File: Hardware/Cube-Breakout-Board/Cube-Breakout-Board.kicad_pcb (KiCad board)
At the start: 2 copper layers, 72.1 x 102.6 mm, 9 parts, among them J1 Pixhawk_Cube_DF17_80_Pin_Grou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, J2 Pixhawk_Cube_DF17_80_Pin_Grou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, J3 Conn_01x30, J4 Conn_01x22, J5 Conn_01x30

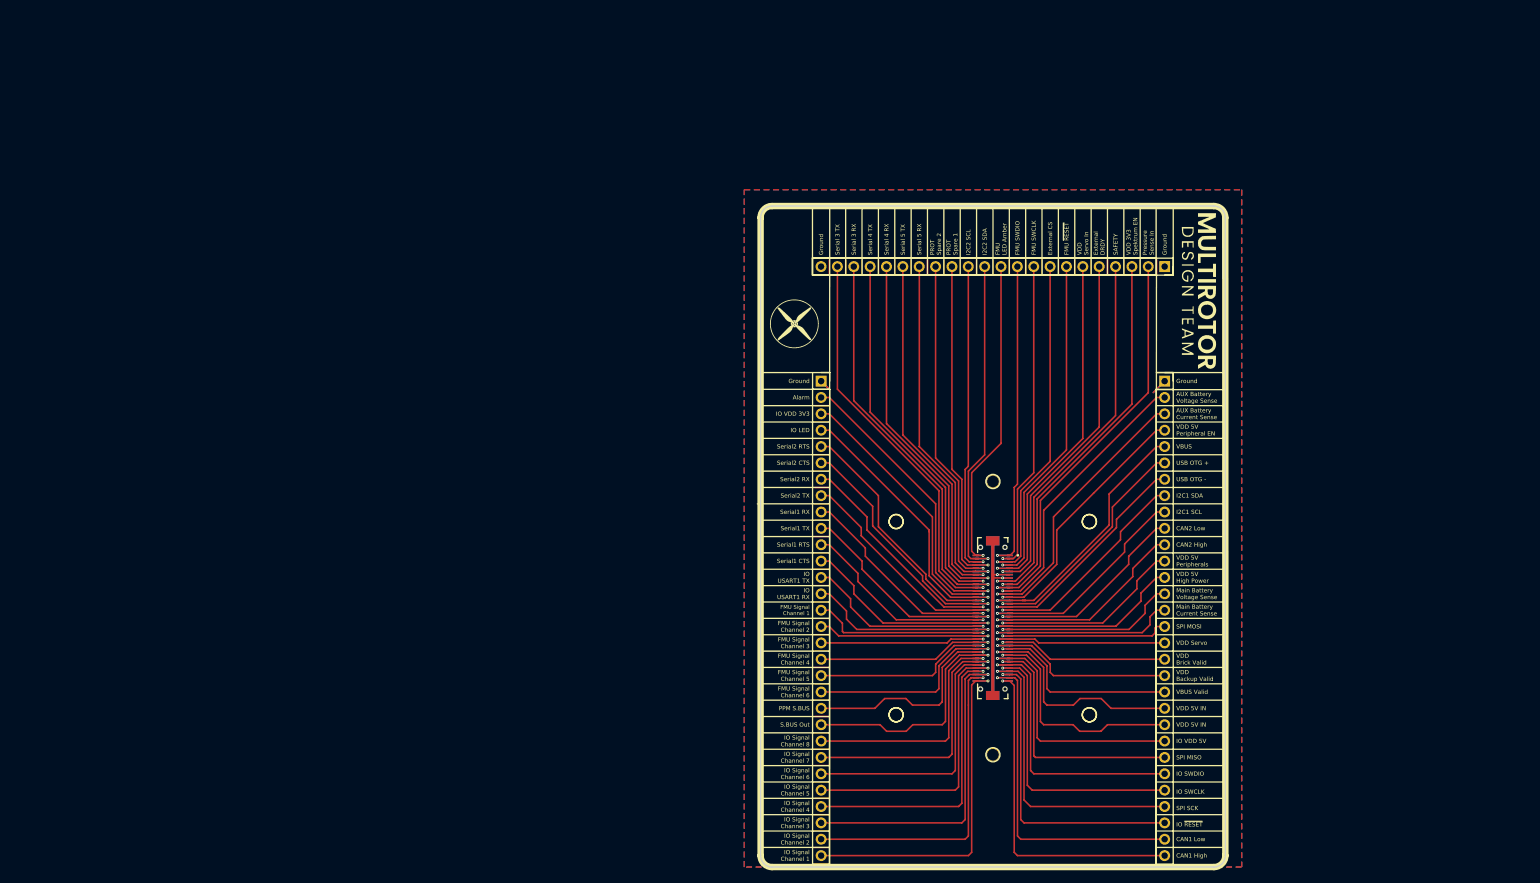
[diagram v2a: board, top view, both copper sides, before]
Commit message: Added dimensions to PCB
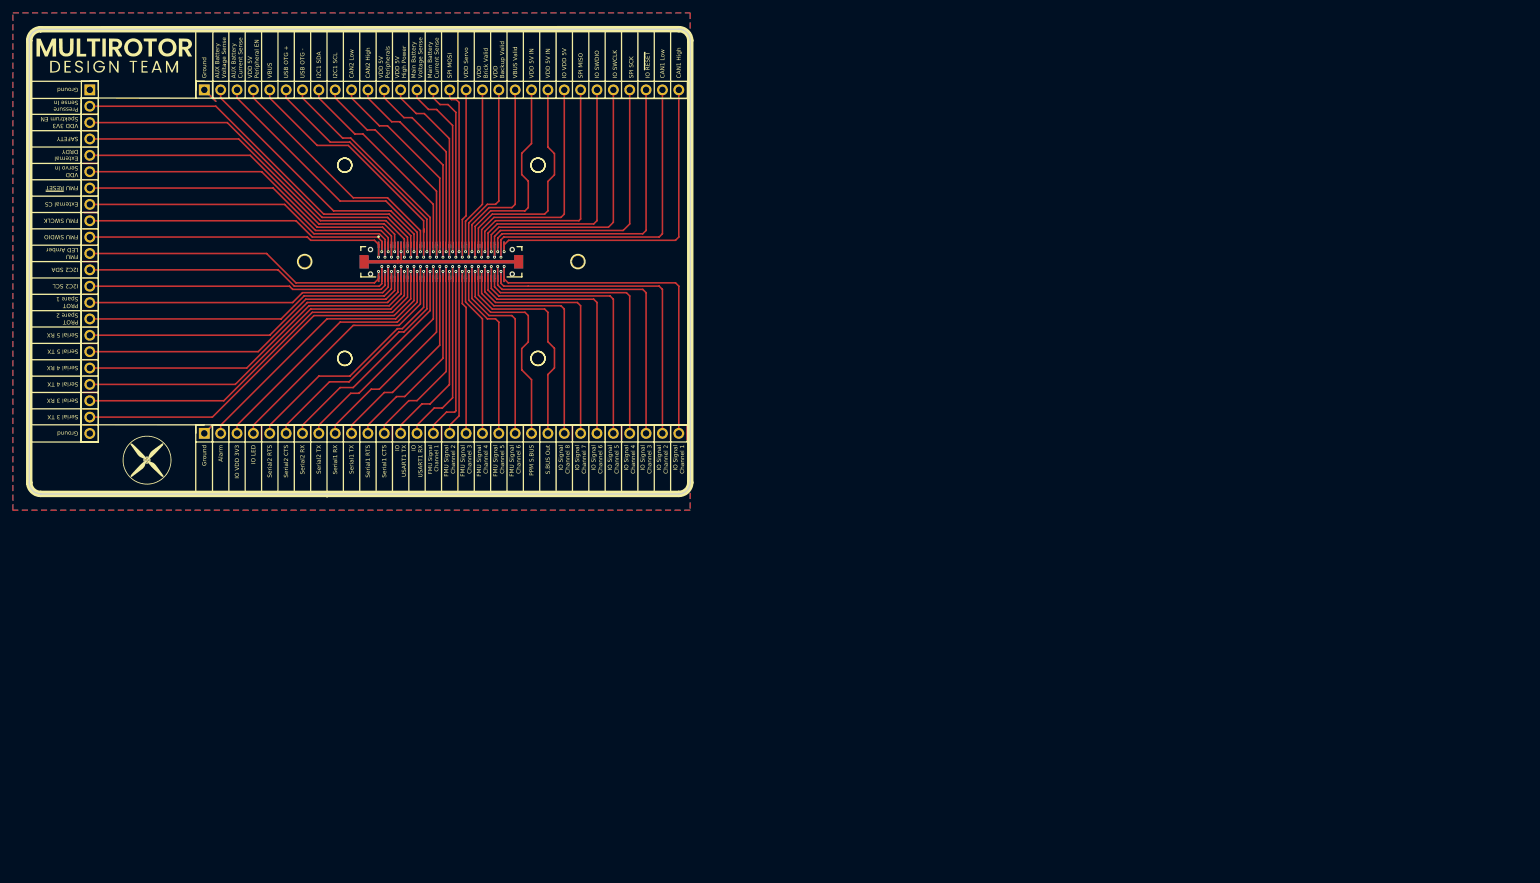
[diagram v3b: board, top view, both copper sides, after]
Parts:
- moved G*** 172.4 mm to (70.6, 25.4), turned to 0 degrees
- moved J4 169.1 mm to (66.8, 30.7), turned to 0 degrees
- moved J5 155.8 mm to (84.6, 30.7), turned to 90 degrees
- moved ? 112.9 mm to (99.1, 57.4), turned to 180 degrees
- moved J1 101.9 mm to (121.4, 57.4), turned to 180 degrees
- moved J2 101.9 mm to (121.4, 57.4), turned to 180 degrees
- moved G*** 101.3 mm to (76.8, 88.2), turned to 90 degrees
- moved ? 99.9 mm to (141.5, 57.4), turned to 180 degrees
- moved J3 96.1 mm to (84.6, 84.1), turned to 90 degrees
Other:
- board size 72.1 x 102.6 mm -> 102.6 x 72.1 mm
